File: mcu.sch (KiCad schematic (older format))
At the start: 28 parts, among them J4 Conn_01x04_Male, Q34 NX7002AK, SW21 SW_Push, SW22 SW_Push, U4 USBUF, U5 STM32F411RCT6, U7 LTV-357T, Y1 8MHz

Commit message: multiple schematic and pcb changes
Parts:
- removed Y1: 8MHz, Oscillators:Oscillator_SMD_EuroQuartz_XO53-4pin_5.0x3.2mm_HandSoldering, symbol Crystal
- added TP1, TP2, TP3, TP4, TP5: TEST, Connectors_TestPoints:Test_Point_Pad_d4.0mm, symbol TEST
- added Y1: 8MHz, Oscillators:Oscillator_SMD_EuroQuartz_XO53-4pin_5.0x3.2mm_HandSoldering, symbol Crystal_GND24
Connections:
- wire segments 119 -> 128
- no-connect marks 1 -> 3
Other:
- moved on the sheet: C14
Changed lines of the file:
@@
 Wire Wire Line
 	14600 3400 14800 3400
-Text HLabel 3800 4900 0    60   Input ~ 0
+Text HLabel 3800 5700 0    60   Input ~ 0
 BUTTON1
-Text HLabel 3800 5000 0    60   Input ~ 0
+Text HLabel 3800 5800 0    60   Input ~ 0
 BUTTON2
 Text HLabel 3800 5500 0    60   Input ~ 0
@@
 ROTARY2_B
 Wire Wire Line
-	3800 4900 5100 4900
-Wire Wire Line
-	3800 5000 5100 5000
+	3800 5700 5100 5700
+Wire Wire Line
+	3800 5800 5100 5800
 Wire Wire Line
 	5100 5500 3800 5500
@@
 $EndComp
 Wire Wire Line
-	2200 4000 5100 4000
+	2000 4000 5100 4000
 Wire Wire Line
 	5100 4100 2700 4100
@@
 	4800 2300 4800 2400
 $Comp
-L Crystal Y1
-U 1 1 5A2F6493
-P 2450 4300
-F 0 "Y1" H 2450 4450 50  0000 C CNN
-F 1 "8MHz" H 2450 4150 50  0000 C CNN
-F 2 "Oscillators:Oscillator_SMD_EuroQuartz_XO53-4pin_5.0x3.2mm_HandSoldering" H 2450 4300 50  0001 C CNN
-F 3 "" H 2450 4300 50  0001 C CNN
-	1    2450 4300
-	1    0    0    -1
-$EndComp
-$Comp
 L C_Small C14
 U 1 1 5A2F66FC
-P 2200 4600
-F 0 "C14" H 2300 4650 50  0000 L CNN
-F 1 "27pF" H 2300 4550 50  0000 L CNN
-F 2 "Capacitors_SMD:C_0603" H 2200 4600 50  0001 C CNN
-F 3 "" H 2200 4600 50  0001 C CNN
-	1    2200 4600
+P 2000 4600
+F 0 "C14" H 2100 4650 50  0000 L CNN
+F 1 "27pF" H 2100 4550 50  0000 L CNN
+F 2 "Capacitors_SMD:C_0603" H 2000 4600 50  0001 C CNN
+F 3 "" H 2000 4600 50  0001 C CNN
+	1    2000 4600
 	1    0    0    -1
 $EndComp
@@
 $EndComp
 Wire Wire Line
-	2200 4000 2200 4500
-Wire Wire Line
-	2300 4300 2200 4300
-Connection ~ 2200 4300
-Wire Wire Line
-	2600 4300 2700 4300
+	2000 4000 2000 4500
+Wire Wire Line
+	2200 4300 2000 4300
+Connection ~ 2000 4300
+Wire Wire Line
+	2500 4300 2700 4300
 Wire Wire Line
 	2700 4100 2700 4500
@@
 L GND #PWR0107
 U 1 1 5A2F6BC6
-P 2200 4800
-F 0 "#PWR0107" H 2200 4550 50  0001 C CNN
-F 1 "GND" H 2200 4650 50  0000 C CNN
-F 2 "" H 2200 4800 50  0001 C CNN
-F 3 "" H 2200 4800 50  0001 C CNN
-	1    2200 4800
+P 2000 4800
+F 0 "#PWR0107" H 2000 4550 50  0001 C CNN
+F 1 "GND" H 2000 4650 50  0000 C CNN
+F 2 "" H 2000 4800 50  0001 C CNN
+F 3 "" H 2000 4800 50  0001 C CNN
+	1    2000 4800
 	1    0    0    -1
 $EndComp
@@
 	2700 4700 2700 4800
 Wire Wire Line
-	2200 4700 2200 4800
+	2000 4700 2000 4800
 $Comp
 L C_Small C13
@@
 Text Label 4850 3500 0    60   ~ 0
 VCAP
-Text Label 2200 4000 0    60   ~ 0
+Text Label 2000 4000 0    60   ~ 0
 XTAL1
 Text Label 2700 4100 0    60   ~ 0
@@
 Text Label 5000 6500 1    60   ~ 0
 UART_RX
+$Comp
+L TEST TP1
+U 1 1 5A5053B7
+P 11550 4900
+F 0 "TP1" V 11550 5100 50  0000 L CNN
+F 1 "TEST" V 11500 5350 50  0001 L CNN
+F 2 "Connectors_TestPoints:Test_Point_Pad_d4.0mm" H 11550 4900 50  0001 C CNN
+F 3 "" H 11550 4900 50  0001 C CNN
+	1    11550 4900
+	0    1    1    0
+$EndComp
+$Comp
+L TEST TP2
+U 1 1 5A50623C
+P 11650 5000
+F 0 "TP2" V 11650 5200 50  0000 L CNN
+F 1 "TEST" V 11600 5450 50  0001 L CNN
+F 2 "Connectors_TestPoints:Test_Point_Pad_d4.0mm" H 11650 5000 50  0001 C CNN
+F 3 "" H 11650 5000 50  0001 C CNN
+	1    11650 5000
+	0    1    1    0
+$EndComp
+$Comp
+L TEST TP3
+U 1 1 5A5062AA
+P 11550 5100
+F 0 "TP3" V 11550 5300 50  0000 L CNN
+F 1 "TEST" V 11500 5550 50  0001 L CNN
+F 2 "Connectors_TestPoints:Test_Point_Pad_d4.0mm" H 11550 5100 50  0001 C CNN
+F 3 "" H 11550 5100 50  0001 C CNN
+	1    11550 5100
+	0    1    1    0
+$EndComp
+Wire Wire Line
+	11550 4900 10900 4900
+Wire Wire Line
+	11650 5000 10900 5000
+Wire Wire Line
+	11550 5100 10900 5100
+$Comp
+L TEST TP4
+U 1 1 5A506644
+P 4800 4900
+F 0 "TP4" V 4800 5100 50  0000 L CNN
+F 1 "TEST" V 4750 5350 50  0001 L CNN
+F 2 "Connectors_TestPoints:Test_Point_Pad_d4.0mm" H 4800 4900 50  0001 C CNN
+F 3 "" H 4800 4900 50  0001 C CNN
+	1    4800 4900
+	0    -1   1    0
+$EndComp
+$Comp
+L TEST TP5
+U 1 1 5A507FC1
+P 4900 5000
+F 0 "TP5" V 4900 5200 50  0000 L CNN
+F 1 "TEST" V 4850 5450 50  0001 L CNN
+F 2 "Connectors_TestPoints:Test_Point_Pad_d4.0mm" H 4900 5000 50  0001 C CNN
+F 3 "" H 4900 5000 50  0001 C CNN
+	1    4900 5000
+	0    -1   1    0
+$EndComp
+Wire Wire Line
+	5100 4900 4800 4900
+Wire Wire Line
+	5100 5000 4900 5000
+NoConn ~ 10900 4800
+NoConn ~ 5100 4300
+$Comp
+L Crystal_GND24 Y1
+U 1 1 5A53F0EA
+P 2350 4300
+F 0 "Y1" H 2050 4500 50  0000 L CNN
+F 1 "8MHz" H 2050 4400 50  0000 L CNN
+F 2 "Oscillators:Oscillator_SMD_EuroQuartz_XO53-4pin_5.0x3.2mm_HandSoldering" H 2350 4300 50  0001 C CNN
+F 3 "" H 2350 4300 50  0001 C CNN
+	1    2350 4300
+	1    0    0    -1
+$EndComp
+Wire Wire Line
+	2350 4100 2550 4100
+Wire Wire Line
+	2550 4100 2550 4500
+Wire Wire Line
+	2550 4500 2350 4500
+Wire Wire Line
+	2350 4500 2350 4800
+$Comp
+L GND #PWR?
+U 1 1 5A5423C1
+P 2350 4800
+F 0 "#PWR?" H 2350 4550 50  0001 C CNN
+F 1 "GND" H 2350 4650 50  0000 C CNN
+F 2 "" H 2350 4800 50  0001 C CNN
+F 3 "" H 2350 4800 50  0001 C CNN
+	1    2350 4800
+	1    0    0    -1
+$EndComp
+Connection ~ 2350 4500
 $EndSCHEMATC

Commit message: pcb in development
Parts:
- removed TP5: TEST, Connectors_TestPoints:Test_Point_Pad_d4.0mm, symbol TEST
- added R35: 10K, Resistors_SMD:R_0603, symbol R_Small
- added TP6: TEST, Connectors_TestPoints:Test_Point_Pad_d3.0mm, symbol TEST
- TP1, TP2, TP3, TP4: footprint Connectors_TestPoints:Test_Point_Pad_d4.0mm -> Connectors_TestPoints:Test_Point_Pad_d3.0mm
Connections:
- net BUTTON1: now also U5.2 (PC13/ANTI_TAMP/RTC_AF1); no longer U5.53 (PC12/I2S3_SD/SDIO_CK/SPI3_MOSI)
- net BUTTON2: now also U5.53 (PC12/I2S3_SD/SDIO_CK/SPI3_MOSI); no longer U5.2 (PC13/ANTI_TAMP/RTC_AF1)
- net GND: now also R35.2
- net LCD_CS: now also U5.29 (I2C2_SCL/I2S2_CK/I2S3_MCK/SDIO_D7/SPI2_SCK/TIM2_CH3/PB10); no longer U5.33 (I2C2_SMBA/I2S2_WS/I2S3_CK/I2S4_WS/SPI2_NSS/SPI3_SCK/SPI4_NSS/TIM1_BKIN/PB12)
- net LCD_DC: now also U5.33 (I2C2_SMBA/I2S2_WS/I2S3_CK/I2S4_WS/SPI2_NSS/SPI3_SCK/SPI4_NSS/TIM1_BKIN/PB12); no longer U5.29 (I2C2_SCL/I2S2_CK/I2S3_MCK/SDIO_D7/SPI2_SCK/TIM2_CH3/PB10)
- net LCD_RESET: now also U5.28 (BOOT1/PB2), R35.1; no longer U5.39 (PC8/SDIO_D0/TIM3_CH3/USART6_CK)
- net ROTARY1_A: now also U5.3 (PC14/RCC_OSC32_IN); no longer U5.51 (PC10/I2S3_CK/SDIO_D2/SPI3_SCK)
- net ROTARY1_B: now also U5.4 (PC15/ADC1_EXTI15/RCC_OSC32_OUT); no longer U5.52 (PC11/ADC1_EXTI11/I2S3_ext_SD/SDIO_D3/SPI3_MISO)
- net ROTARY2_A: now also U5.51 (PC10/I2S3_CK/SDIO_D2/SPI3_SCK); no longer U5.3 (PC14/RCC_OSC32_IN)
- net ROTARY2_B: now also U5.52 (PC11/ADC1_EXTI11/I2S3_ext_SD/SDIO_D3/SPI3_MISO); no longer U5.4 (PC15/ADC1_EXTI15/RCC_OSC32_OUT)
- new net: TP6.1, U5.39 (PC8/SDIO_D0/TIM3_CH3/USART6_CK)
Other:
- moved on the sheet: TP1, TP2, TP3
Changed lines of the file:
@@
 Text HLabel 12500 3400 2    60   Output ~ 0
 PWM_GREEN[1..4]
-Text Label 11000 5200 0    60   ~ 0
+Text Label 11200 5200 0    60   ~ 0
 PWM_BLUE1
-Text Label 11000 5300 0    60   ~ 0
+Text Label 11200 5300 0    60   ~ 0
 PWM_BLUE2
-Text Label 11000 5400 0    60   ~ 0
+Text Label 11200 5400 0    60   ~ 0
 PWM_BLUE3
-Text Label 11000 5500 0    60   ~ 0
+Text Label 11200 5500 0    60   ~ 0
 PWM_BLUE4
 Entry Wire Line
@@
 Wire Wire Line
 	14600 3400 14800 3400
+Text HLabel 3800 5800 0    60   Input ~ 0
+BUTTON1
 Text HLabel 3800 5700 0    60   Input ~ 0
-BUTTON1
-Text HLabel 3800 5800 0    60   Input ~ 0
 BUTTON2
+Text HLabel 3800 5900 0    60   Input ~ 0
+ROTARY1_A
+Text HLabel 3800 6000 0    60   Input ~ 0
+ROTARY1_B
 Text HLabel 3800 5500 0    60   Input ~ 0
-ROTARY1_A
+ROTARY2_A
 Text HLabel 3800 5600 0    60   Input ~ 0
-ROTARY1_B
-Text HLabel 3800 5900 0    60   Input ~ 0
-ROTARY2_A
-Text HLabel 3800 6000 0    60   Input ~ 0
 ROTARY2_B
 Wire Wire Line
@@
 Text HLabel 12500 5900 2    60   Output ~ 0
 LCD_LIGHT
+Text HLabel 12500 5700 2    60   Output ~ 0
+LCD_DC
 Text HLabel 12500 5600 2    60   Output ~ 0
-LCD_DC
-Text HLabel 12500 5700 2    60   Output ~ 0
 LCD_CS
-Text HLabel 3800 5300 0    60   Output ~ 0
+Text HLabel 12500 4800 2    60   Output ~ 0
 LCD_RESET
 Wire Wire Line
@@
 Wire Wire Line
 	10900 6000 12500 6000
-Wire Wire Line
-	5100 5300 3800 5300
 $Comp
 L C_Small C12
@@
 L TEST TP1
 U 1 1 5A5053B7
-P 11550 4900
-F 0 "TP1" V 11550 5100 50  0000 L CNN
-F 1 "TEST" V 11500 5350 50  0001 L CNN
-F 2 "Connectors_TestPoints:Test_Point_Pad_d4.0mm" H 11550 4900 50  0001 C CNN
-F 3 "" H 11550 4900 50  0001 C CNN
-	1    11550 4900
+P 11850 4900
+F 0 "TP1" V 11850 5100 50  0000 L CNN
+F 1 "TEST" V 11800 5350 50  0001 L CNN
+F 2 "Connectors_TestPoints:Test_Point_Pad_d3.0mm" H 11850 4900 50  0001 C CNN
+F 3 "" H 11850 4900 50  0001 C CNN
+	1    11850 4900
 	0    1    1    0
 $EndComp
@@
 L TEST TP2
 U 1 1 5A50623C
-P 11650 5000
-F 0 "TP2" V 11650 5200 50  0000 L CNN
-F 1 "TEST" V 11600 5450 50  0001 L CNN
-F 2 "Connectors_TestPoints:Test_Point_Pad_d4.0mm" H 11650 5000 50  0001 C CNN
-F 3 "" H 11650 5000 50  0001 C CNN
-	1    11650 5000
+P 11950 5000
+F 0 "TP2" V 11950 5200 50  0000 L CNN
+F 1 "TEST" V 11900 5450 50  0001 L CNN
+F 2 "Connectors_TestPoints:Test_Point_Pad_d3.0mm" H 11950 5000 50  0001 C CNN
+F 3 "" H 11950 5000 50  0001 C CNN
+	1    11950 5000
 	0    1    1    0
 $EndComp
@@
 L TEST TP3
 U 1 1 5A5062AA
-P 11550 5100
-F 0 "TP3" V 11550 5300 50  0000 L CNN
-F 1 "TEST" V 11500 5550 50  0001 L CNN
-F 2 "Connectors_TestPoints:Test_Point_Pad_d4.0mm" H 11550 5100 50  0001 C CNN
-F 3 "" H 11550 5100 50  0001 C CNN
-	1    11550 5100
+P 11850 5100
+F 0 "TP3" V 11850 5300 50  0000 L CNN
+F 1 "TEST" V 11800 5550 50  0001 L CNN
+F 2 "Connectors_TestPoints:Test_Point_Pad_d3.0mm" H 11850 5100 50  0001 C CNN
+F 3 "" H 11850 5100 50  0001 C CNN
+	1    11850 5100
 	0    1    1    0
 $EndComp
 Wire Wire Line
-	11550 4900 10900 4900
-Wire Wire Line
-	11650 5000 10900 5000
-Wire Wire Line
-	11550 5100 10900 5100
+	11850 4900 10900 4900
+Wire Wire Line
+	11950 5000 10900 5000
+Wire Wire Line
+	11850 5100 10900 5100
 $Comp
 L TEST TP4
@@
 F 0 "TP4" V 4800 5100 50  0000 L CNN
 F 1 "TEST" V 4750 5350 50  0001 L CNN
-F 2 "Connectors_TestPoints:Test_Point_Pad_d4.0mm" H 4800 4900 50  0001 C CNN
+F 2 "Connectors_TestPoints:Test_Point_Pad_d3.0mm" H 4800 4900 50  0001 C CNN
 F 3 "" H 4800 4900 50  0001 C CNN
 	1    4800 4900
 	0    -1   1    0
 $EndComp
-$Comp
-L TEST TP5
-U 1 1 5A507FC1
-P 4900 5000
-F 0 "TP5" V 4900 5200 50  0000 L CNN
-F 1 "TEST" V 4850 5450 50  0001 L CNN
-F 2 "Connectors_TestPoints:Test_Point_Pad_d4.0mm" H 4900 5000 50  0001 C CNN
-F 3 "" H 4900 5000 50  0001 C CNN
-	1    4900 5000
-	0    -1   1    0
-$EndComp
 Wire Wire Line
 	5100 4900 4800 4900
-Wire Wire Line
-	5100 5000 4900 5000
-NoConn ~ 10900 4800
 NoConn ~ 5100 4300
 $Comp
@@
 	2350 4500 2350 4800
 $Comp
-L GND #PWR?
+L GND #PWR0119
 U 1 1 5A5423C1
 P 2350 4800
-F 0 "#PWR?" H 2350 4550 50  0001 C CNN
+F 0 "#PWR0119" H 2350 4550 50  0001 C CNN
 F 1 "GND" H 2350 4650 50  0000 C CNN
 F 2 "" H 2350 4800 50  0001 C CNN
@@
 $EndComp
 Connection ~ 2350 4500
+$Comp
+L R_Small R35
+U 1 1 5A528706
+P 11000 6200
+F 0 "R35" H 11050 6250 50  0000 L CNN
+F 1 "10K" H 11050 6150 50  0000 L CNN
+F 2 "Resistors_SMD:R_0603" H 11000 6200 50  0001 C CNN
+F 3 "" H 11000 6200 50  0001 C CNN
+	1    11000 6200
+	1    0    0    -1
+$EndComp
+$Comp
+L GND #PWR0120
+U 1 1 5A528F88
+P 11000 6300
+F 0 "#PWR0120" H 11000 6050 50  0001 C CNN
+F 1 "GND" H 11000 6150 50  0000 C CNN
+F 2 "" H 11000 6300 50  0001 C CNN
+F 3 "" H 11000 6300 50  0001 C CNN
+	1    11000 6300
+	1    0    0    -1
+$EndComp
+Wire Wire Line
+	11000 6100 11000 4800
+Wire Wire Line
+	10900 4800 12500 4800
+Connection ~ 11000 4800
+Wire Wire Line
+	5100 5300 4800 5300
+$Comp
+L TEST TP6
+U 1 1 5A52B56E
+P 4800 5300
+F 0 "TP6" V 4800 5500 50  0000 L CNN
+F 1 "TEST" V 4750 5750 50  0001 L CNN
+F 2 "Connectors_TestPoints:Test_Point_Pad_d3.0mm" H 4800 5300 50  0001 C CNN
+F 3 "" H 4800 5300 50  0001 C CNN
+	1    4800 5300
+	0    -1   1    0
+$EndComp
+NoConn ~ 5100 5000
 $EndSCHEMATC

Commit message: commiting before bulk led schematic symbol change
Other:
- moved on the sheet: C10, C11, C12, C13, C14, C15, C4, C5, C6, C7, C8, C9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

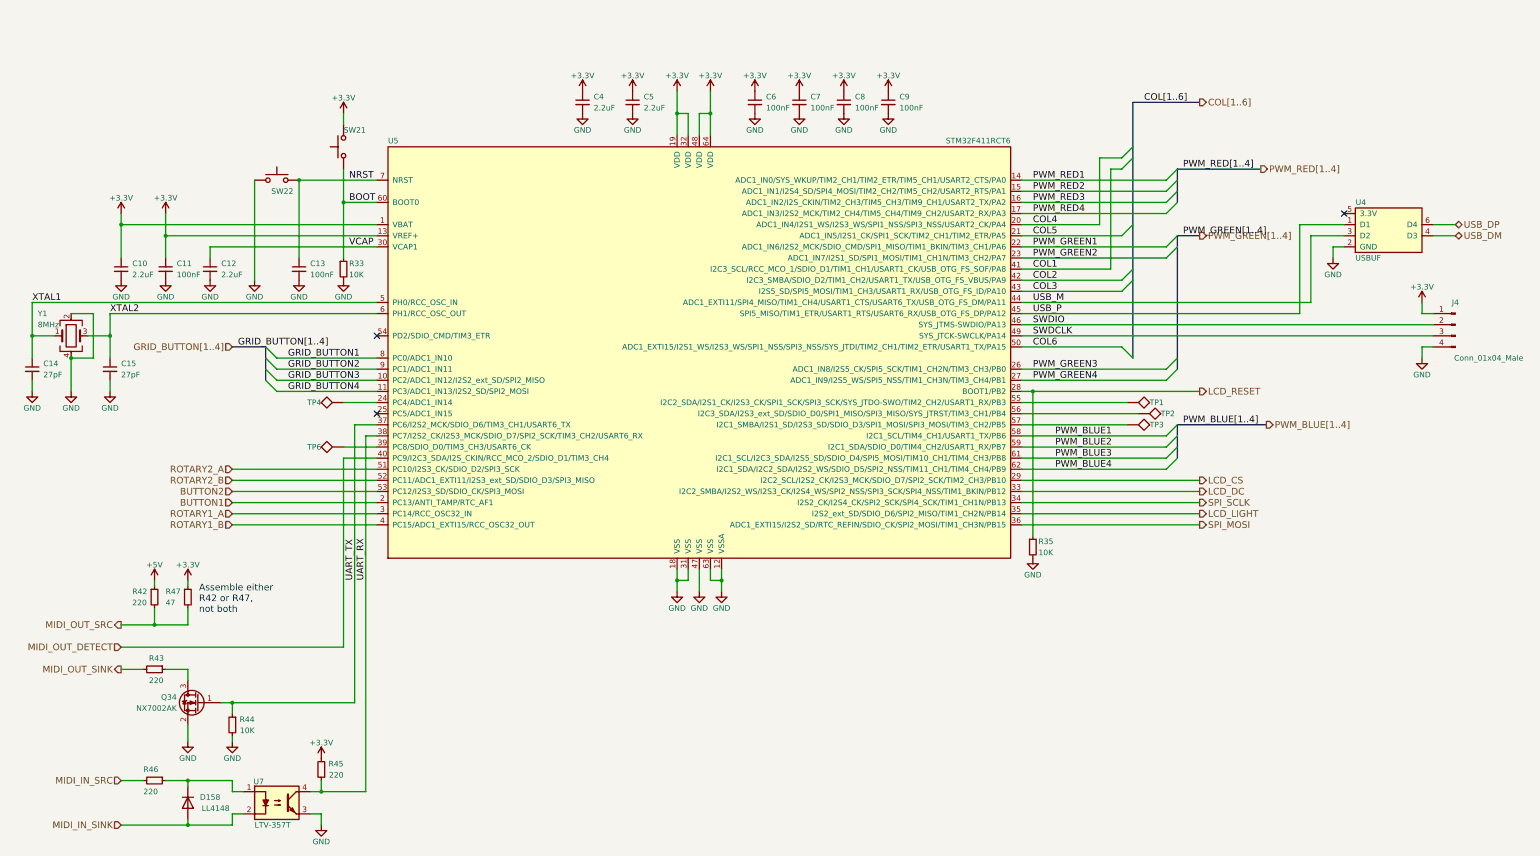
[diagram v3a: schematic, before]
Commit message: successfuly changed component symbols and net names, further developed pcb
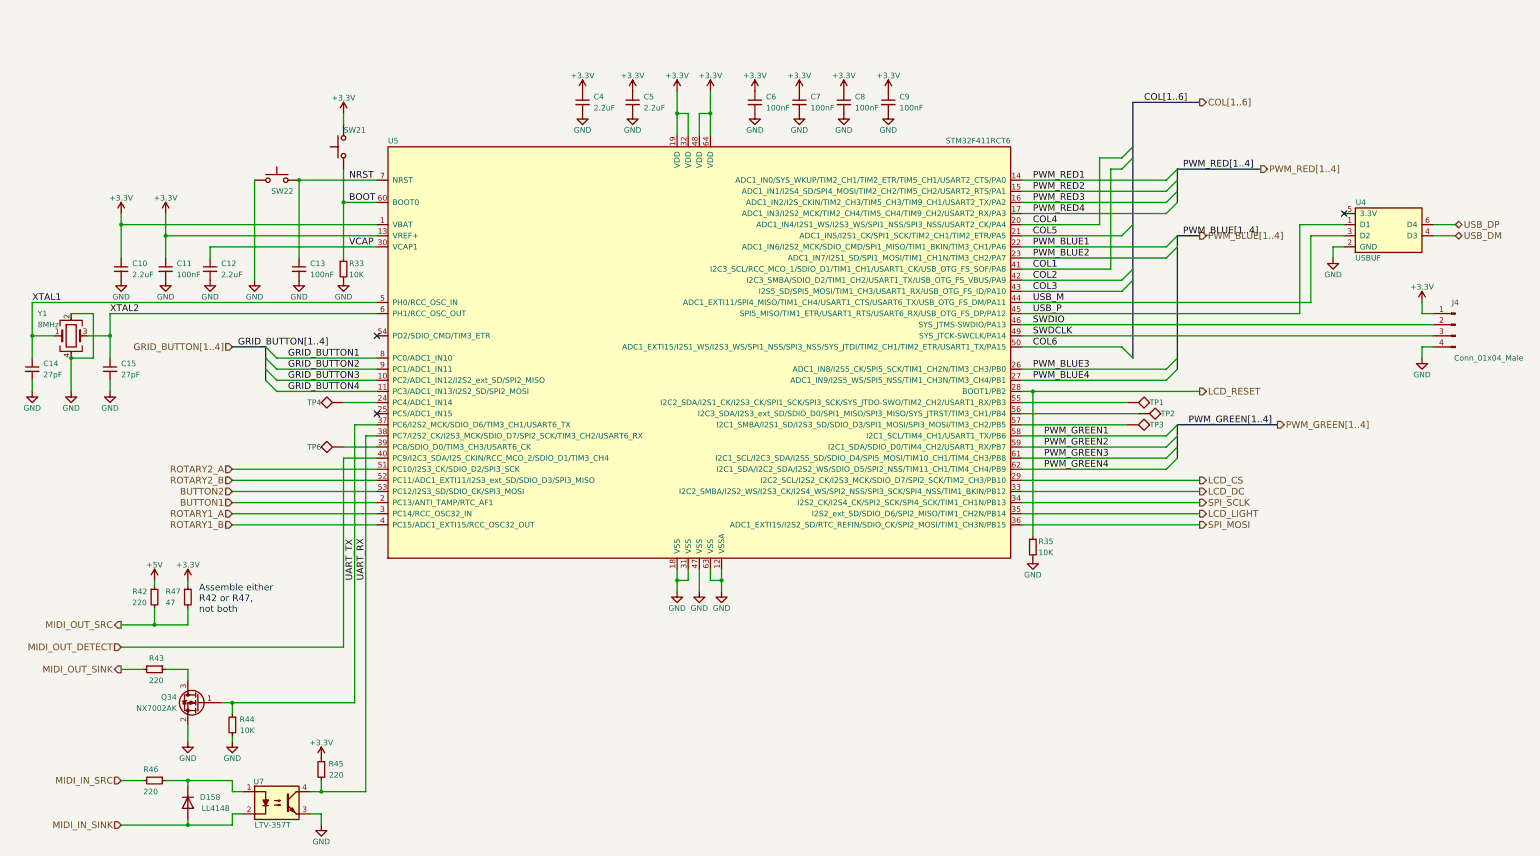
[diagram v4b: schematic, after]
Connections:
- net PWM_BLUE1: now also U5.22 (ADC1_IN6/I2S2_MCK/SDIO_CMD/SPI1_MISO/TIM1_BKIN/TIM3_CH1/PA6); no longer U5.58 (I2C1_SCL/TIM4_CH1/USART1_TX/PB6)
- net PWM_BLUE2: now also U5.23 (ADC1_IN7/I2S1_SD/SPI1_MOSI/TIM1_CH1N/TIM3_CH2/PA7); no longer U5.59 (I2C1_SDA/SDIO_D0/TIM4_CH2/USART1_RX/PB7)
- net PWM_BLUE3: now also U5.26 (ADC1_IN8/I2S5_CK/SPI5_SCK/TIM1_CH2N/TIM3_CH3/PB0); no longer U5.61 (I2C1_SCL/I2C3_SDA/I2S5_SD/SDIO_D4/SPI5_MOSI/TIM10_CH1/TIM4_CH3/PB8)
- net PWM_BLUE4: now also U5.27 (ADC1_IN9/I2S5_WS/SPI5_NSS/TIM1_CH3N/TIM3_CH4/PB1); no longer U5.62 (I2C1_SDA/I2C2_SDA/I2S2_WS/SDIO_D5/SPI2_NSS/TIM11_CH1/TIM4_CH4/PB9)
- net PWM_GREEN1: now also U5.58 (I2C1_SCL/TIM4_CH1/USART1_TX/PB6); no longer U5.22 (ADC1_IN6/I2S2_MCK/SDIO_CMD/SPI1_MISO/TIM1_BKIN/TIM3_CH1/PA6)
- net PWM_GREEN2: now also U5.59 (I2C1_SDA/SDIO_D0/TIM4_CH2/USART1_RX/PB7); no longer U5.23 (ADC1_IN7/I2S1_SD/SPI1_MOSI/TIM1_CH1N/TIM3_CH2/PA7)
- net PWM_GREEN3: now also U5.61 (I2C1_SCL/I2C3_SDA/I2S5_SD/SDIO_D4/SPI5_MOSI/TIM10_CH1/TIM4_CH3/PB8); no longer U5.26 (ADC1_IN8/I2S5_CK/SPI5_SCK/TIM1_CH2N/TIM3_CH3/PB0)
- net PWM_GREEN4: now also U5.62 (I2C1_SDA/I2C2_SDA/I2S2_WS/SDIO_D5/SPI2_NSS/TIM11_CH1/TIM4_CH4/PB9); no longer U5.27 (ADC1_IN9/I2S5_WS/SPI5_NSS/TIM1_CH3N/TIM3_CH4/PB1)
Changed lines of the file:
@@
 Text HLabel 13050 3350 2    60   Output ~ 0
 PWM_RED[1..4]
+Text Label 11100 5750 0    60   ~ 0
+PWM_GREEN1
+Text Label 11100 5850 0    60   ~ 0
+PWM_GREEN2
+Text Label 11100 5950 0    60   ~ 0
+PWM_GREEN3
+Text Label 11100 6050 0    60   ~ 0
+PWM_GREEN4
+Entry Wire Line
+	12200 4050 12300 3950
+Entry Wire Line
+	12200 4150 12300 4050
+Entry Wire Line
+	12200 5150 12300 5050
+Entry Wire Line
+	12200 5250 12300 5150
+Text HLabel 13200 5650 2    60   Output ~ 0
+PWM_GREEN[1..4]
 Text Label 11000 4050 0    60   ~ 0
-PWM_GREEN1
+PWM_BLUE1
 Text Label 11000 4150 0    60   ~ 0
-PWM_GREEN2
+PWM_BLUE2
 Text Label 11000 5150 0    60   ~ 0
-PWM_GREEN3
+PWM_BLUE3
 Text Label 11000 5250 0    60   ~ 0
-PWM_GREEN4
-Entry Wire Line
-	12200 4050 12300 3950
-Entry Wire Line
-	12200 4150 12300 4050
-Entry Wire Line
-	12200 5150 12300 5050
-Entry Wire Line
-	12200 5250 12300 5150
+PWM_BLUE4
+Entry Wire Line
+	12200 5750 12300 5650
+Entry Wire Line
+	12200 5850 12300 5750
+Entry Wire Line
+	12200 5950 12300 5850
+Entry Wire Line
+	12200 6050 12300 5950
 Text HLabel 12500 3950 2    60   Output ~ 0
-PWM_GREEN[1..4]
-Text Label 11200 5750 0    60   ~ 0
-PWM_BLUE1
-Text Label 11200 5850 0    60   ~ 0
-PWM_BLUE2
-Text Label 11200 5950 0    60   ~ 0
-PWM_BLUE3
-Text Label 11200 6050 0    60   ~ 0
-PWM_BLUE4
-Entry Wire Line
-	12200 5750 12300 5650
-Entry Wire Line
-	12200 5850 12300 5750
-Entry Wire Line
-	12200 5950 12300 5850
-Entry Wire Line
-	12200 6050 12300 5950
-Text HLabel 13100 5650 2    60   Output ~ 0
 PWM_BLUE[1..4]
 Wire Wire Line
@@
 	10900 6050 12200 6050
 Wire Bus Line
-	12300 5650 13100 5650
+	12300 5650 13200 5650
 Wire Bus Line
 	12300 5650 12300 5950
@@
 	3900 9150 3800 9150
 Wire Wire Line
-	3800 9150 3800 9250
-Wire Wire Line
-	3800 9250 2800 9250
+	3800 9250 3800 9150
+Wire Wire Line
+	2800 9250 3800 9250
 Wire Wire Line
 	3400 9200 3400 9250
@@
 Text Label 12350 3350 0    60   ~ 0
 PWM_RED[1..4]
+Text Label 12400 5650 0    60   ~ 0
+PWM_GREEN[1..4]
 Text Label 12350 3950 0    60   ~ 0
-PWM_GREEN[1..4]
-Text Label 12350 5650 0    60   ~ 0
 PWM_BLUE[1..4]
 Text Label 3850 4950 0    60   ~ 0
